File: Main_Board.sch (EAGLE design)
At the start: 189 parts, among them Q1 CSD17308Q3, Q2 CSD17308Q3, Q3 CSD17308Q3, Q4 CSD17308Q3, Q5 CSD17308Q3, Q6 CSD17308Q3, Q7 CSD17308Q3, U1 RN4020RN4020, U2 LMS8117, U3 5V_BUCK_REG, U4 IMU, U5 STM32F405RGT6, U6 TPA2005D1DGN, U7 BQ40Z60, U8 BQ2947, Y1 MC-30632.768K-E3, Y2 MA-5066-25.0000M-C0

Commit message: Finalized parts
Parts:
- added C14, C21: 4.7uF, SparkFun-Capacitors:CAP0805
- added C22: 150pF, SparkFun-Capacitors:CAP0805
- added C23: 10pF, SparkFun-Capacitors:CAP0805
- added C24: 47uF, BB8:CAP-1206
- added C25: 22uF, SparkFun-Capacitors:CAP0805
- added C53: 100nF, SparkFun-Capacitors:CAP0805
- added C55: 470nF, SparkFun-Capacitors:CAP0805
- added C58, C59: 0.1uF, SparkFun-Capacitors:CAP0805
- added J4: SPEAKER, BB8:2-PIN-JUMPER
- added J5: 5.5x2.1mm Barrel, SparkFun-Connectors:POWER_JACKSMD
- added J6: 9.7uH, BB8:2-PIN-JUMPER
- added L2: 3.3uH, BB8:INDUCTOR-SPM6530
- added Q8: SI9933CDY-PFET, BB8:SI9933CDY-PFET
- added R29: 57.6k, SparkFun-Passives:RESISTOR0805-RES
- added R30: 365k, SparkFun-Passives:RESISTOR0805-RES
- added R31: 113k, SparkFun-Passives:RESISTOR0805-RES
- added R61: 1.3M, SparkFun-Passives:RESISTOR0805-RES
- added R68: 1500, SparkFun-Passives:RESISTOR0805-RES
- added R70: 100k, SparkFun-Passives:RESISTOR0805-RES
- added RFOD: 196, SparkFun-Passives:RESISTOR0805-RES
- added ROS: 20k, SparkFun-Passives:RESISTOR0805-RES
- added U11: CBAT54S-SOT23-3, BB8:CBAT54S-SOT23-3
- added Z5: DDZ16ASF-7, BB8:DDZ16ASF-7
- C101: value (none) -> 270nF
- C102: value (none) -> 2.7nF
- C26, C27: value (none) -> 0.1uF
- CBOOT1, CBOOT2: value (none) -> 10nF
- CCLAMP1, CCLAMP2: value (none) -> 0.47uF
- CCOMM1, CCOMM2: value (none) -> 22nF
- D4: value BLUE -> GREEN
- D7: value 1N4148-0805 -> DIODE-1206; device BB8:1N4148-0805 -> BB8:DIODE-1206
- F1, F2: value F2875CT-ND -> (none)
- J2: value (none) -> SD_WP
- J3: value (none) -> BATTERY
- L3: device SparkFun-Passives:INDUCTOR0805 -> BB8:INDUCTOR-SPM6530
- R32: value (none) -> 66
- R33: value (none) -> 100k
- R34: value (none) -> 4.7k
- Y1: value MC-30632.768K-E3 -> (none)
- Y2: value MA-5066-25.0000M-C0 -> (none)
- renumbered U$10 to U10, U$12 to U12, U$9 to U9
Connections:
- removed net AUDIO_OUT+: U6.OUT+
- removed net AUDIO_OUT-: U6.OUT-
- removed net OUT: C26.1, D4.A, WPC-RX1.OUT
- removed net TRI-STATE: THM2.1, WPC-RX1.TS/CTRL
- removed net VDD_5V: C28.1, U6.VDD
- new net AUDIO+: J4.2, U6.OUT+
- new net AUDIO-: J4.1, U6.OUT-
- new net N$109: C53.2, U$5.CAP
- new net N$115: D4.C, R68.1
- new net N$117: R31.2, R61.1, U$5.FB
- new net N$119: C23.1, R30.2, U$5.VC
- new net N$120: C55.2, U11.P$3
- new net N$123: C24.2, U11.P$1, Z5.A
- new net N$124: C58.1, R33.1, R34.1, R70.1, WPC-RX1.TS/CTRL
- new net N$125: Q8G$1.G, Q8G$2.G, WPC-RX1.!AD-EN
- new net N$126: R34.2, THM2.1
- new net N$127: Q8G$1.S, Q8G$2.S
- new net N$128: C59.1, J5.PWR, Q8G$1.D, WPC-RX1.AD
- new net N$50: C22.1, R30.1
- new net N$51: C21.1, U$5.PWM/SYNC, U$5.VCC
- new net N$52: R29.2, U$5.RT
- new net N$53: C55.1, L2.2, U$5.SW
- new net WIRELESS_OUT_5V: C14.1, C26.1, D4.A, L2.1, Q8G$2.D, U$5.!SD, U$5.V_IN, WPC-RX1.OUT
- net 5V: now also C28.1, U6.VDD
- net AC2: now also J6.1
- net GND: now also C14.2, C21.2, C22.2, C23.2, C24.1, C25.2, C58.2, C59.2, J5.GND, J5.GNDBREAK, R29.1, R31.1, R70.2, RFOD.2, U$5.PGND, U$5.SGND, U11.P$2, Z5.C; no longer WPC-RX1.AD
- net N$59: now also J6.2
- net N$61: now also RFOD.1, ROS.1; no longer R33.1, R34.1
- net N$62: now also ROS.2; no longer R34.2
- net N$63: now also R68.2; no longer D4.C
- net PACK+: now also C25.1, C53.1, R61.2, U$5.V_OUT
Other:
- note added: "+15V Out, goes to Pack+"
- note added: "Is this okay kyle?"
- note added: "Wireless Charging Receiver and 5 to 15V Converter"
- note removed: "Coil goes here"
- note removed: "Wireless Charging Receiver"
- moved on the sheet: C28, D4, R33, R34, THM2, U$5

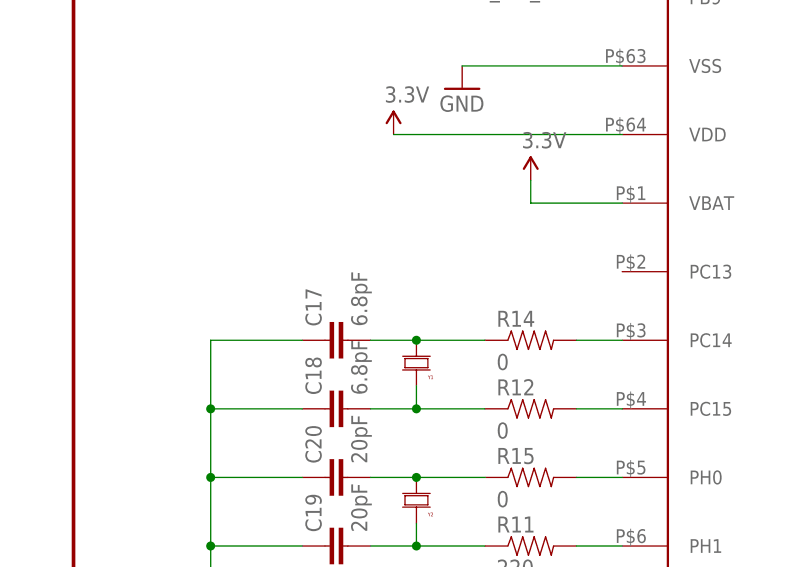
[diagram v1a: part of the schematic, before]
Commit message: added heartbeat LED to PC13
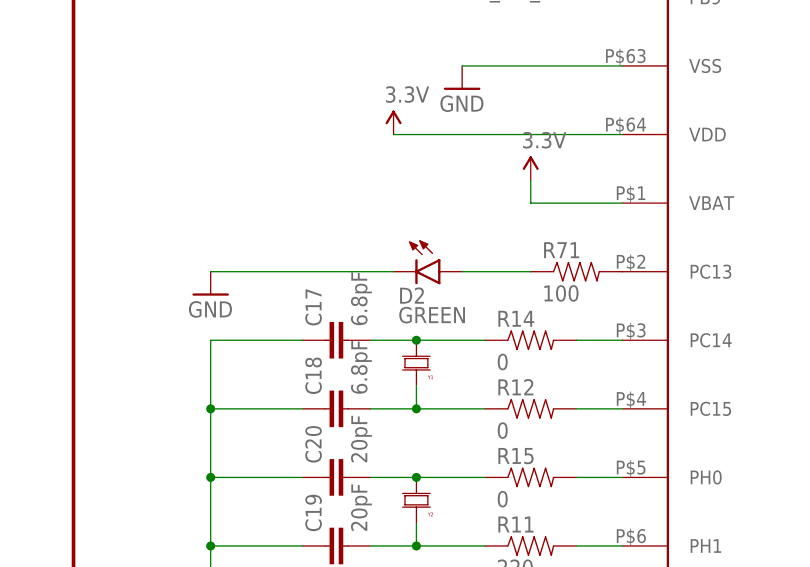
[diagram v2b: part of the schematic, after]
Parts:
- added D2: GREEN, SparkFun-LED:LED-BLUE0603
- added R71: 100, SparkFun-Resistors:RESISTOR0805-RES
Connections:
- new net N$129: R71.2, U5.PC13
- new net N$130: D2.A, R71.1
- net GND: now also D2.C
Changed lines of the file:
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@@
 <part name="J6" library="BB8" deviceset="2-PIN-JUMPER" device="" value="9.7uH"/>
 <part name="C24" library="BB8" deviceset="CAP-1206" device="" value="47uF"/>
+<part name="R71" library="SparkFun-Resistors" deviceset="RESISTOR" device="0805-RES" value="100"/>
+<part name="D2" library="SparkFun-LED" deviceset="LED-BLUE" device="0603" value="GREEN"/>
+<part name="GND48" library="SparkFun-Aesthetics" deviceset="GND" device=""/>
 </parts>
 <sheets>
@@
 <instance part="J6" gate="G$1" x="828.04" y="88.9"/>
 <instance part="C24" gate="G$1" x="1158.24" y="60.96" rot="R180"/>
+<instance part="R71" gate="G$1" x="330.2" y="134.62"/>
+<instance part="D2" gate="G$1" x="314.96" y="134.62" rot="R270"/>
+<instance part="GND48" gate="1" x="289.56" y="132.08"/>
 </instances>
 <busses>
@@
 <junction x="817.88" y="147.32"/>
 </segment>
+<segment>
+<pinref part="D2" gate="G$1" pin="C"/>
+<pinref part="GND48" gate="1" pin="GND"/>
+<wire x1="309.88" y1="134.62" x2="289.56" y2="134.62" width="0.1524" layer="91"/>
+</segment>
 </net>
 <net name="N$1" class="0">
@@
 </segment>
 </net>
+<net name="N$129" class="0">
+<segment>
+<pinref part="U5" gate="G$1" pin="PC13"/>
+<pinref part="R71" gate="G$1" pin="2"/>
+</segment>
+</net>
+<net name="N$130" class="0">
+<segment>
+<pinref part="R71" gate="G$1" pin="1"/>
+<pinref part="D2" gate="G$1" pin="A"/>
+<wire x1="325.12" y1="134.62" x2="317.5" y2="134.62" width="0.1524" layer="91"/>
+</segment>
+</net>

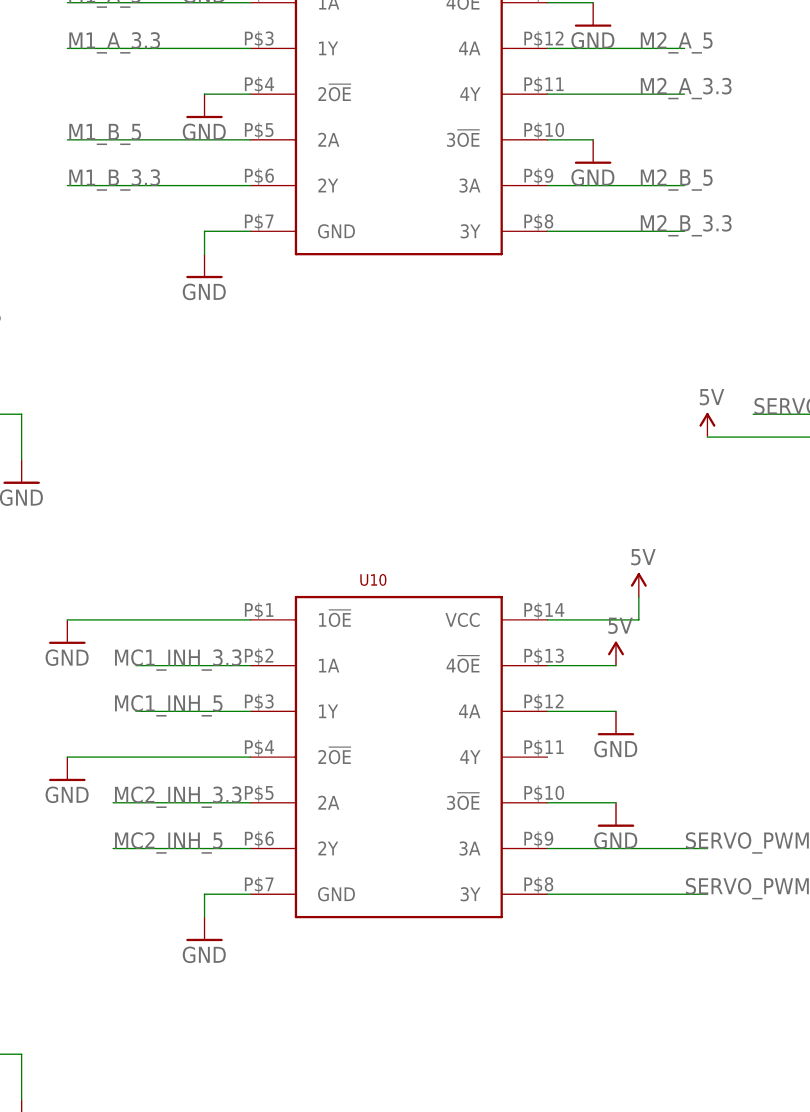
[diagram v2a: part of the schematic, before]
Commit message: Replaced inductor in buck regulator
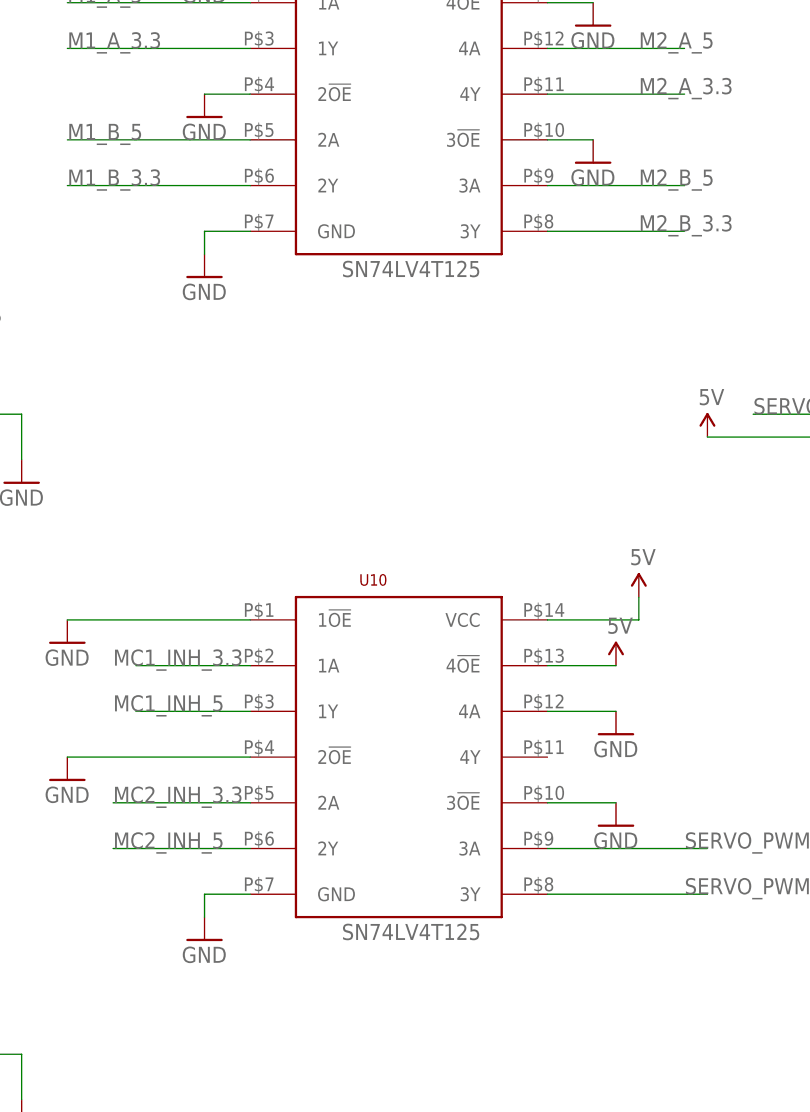
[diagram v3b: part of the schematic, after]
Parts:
- L1: device SparkFun-Passives:INDUCTOR0805 -> BB8:SRN840-101M
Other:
- note removed: "Change to Digikey Part#: SRN8040-101MCT-ND"
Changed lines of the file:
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@@
 <part name="U$8" library="BB8" deviceset="CAP_POL_PAN" device="" value="100uF"/>
 <part name="Z1" library="BB8" deviceset="SCHOTTKY_DIODE" device=""/>
-<part name="L1" library="SparkFun-Passives" deviceset="INDUCTOR" device="0805" value="100uH"/>
+<part name="L1" library="BB8" deviceset="SRN840-101M" device="" value="100uH"/>
 <part name="U$11" library="BB8" deviceset="CAP_POL_PAN" device="" value="470uF"/>
 <part name="GND34" library="SparkFun-Aesthetics" deviceset="GND" device=""/>
@@
 <text x="1663.7" y="-271.78" size="1.778" layer="97">also known as ground</text>
 <text x="1671.32" y="-248.92" size="1.778" layer="97">charging +</text>
-<text x="-5.08" y="-172.72" size="1.778" layer="98">Change to Digikey Part#:
-SRN8040-101MCT-ND</text>
 <text x="462.28" y="-220.98" size="1.778" layer="98">Should possibly be .065K</text>
 <text x="1056.64" y="101.6" size="1.778" layer="97">Is this okay kyle?</text>
@@
 <instance part="SUPPLY13" gate="G$1" x="-71.12" y="-91.44"/>
 <instance part="GND18" gate="1" x="-71.12" y="-106.68"/>
-<instance part="U9" gate="G$1" x="157.48" y="129.54"/>
+<instance part="U9" gate="G$1" x="167.64" y="114.3"/>
 <instance part="GND19" gate="1" x="147.32" y="93.98"/>
 <instance part="GND20" gate="1" x="147.32" y="111.76"/>
@@
 <instance part="GND23" gate="1" x="190.5" y="106.68"/>
 <instance part="SUPPLY14" gate="G$1" x="193.04" y="132.08"/>
-<instance part="U10" gate="G$1" x="157.48" y="55.88"/>
+<instance part="U10" gate="G$1" x="167.64" y="40.64"/>
 <instance part="SUPPLY15" gate="G$1" x="195.58" y="58.42"/>
 <instance part="GND24" gate="1" x="147.32" y="20.32"/>
@@
 </schematic>
 </drawing>
-<compatibility>
-<note version="6.3" minversion="6.2.2" severity="warning">
-Since Version 6.2.2 text objects can contain more than one line,
-which will not be processed correctly with this version.
-</note>
-</compatibility>
 </eagle>

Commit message: Renumbered ALL elements
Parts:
- removed C101: 270nF, SparkFun-Capacitors:CAP0805
- removed C102: 2.7nF, SparkFun-Capacitors:CAP0805
- removed CBOOT1, CBOOT2: 10nF, SparkFun-Capacitors:CAP0805
- removed CCLAMP1, CCLAMP2: 0.47uF, SparkFun-Capacitors:CAP0805
- removed CCOMM1, CCOMM2: 22nF, SparkFun-Capacitors:CAP0805
- removed D7: DIODE-1206, BB8:DIODE-1206
- removed RFOD: 196, SparkFun-Passives:RESISTOR0805-RES
- removed ROS: 20k, SparkFun-Passives:RESISTOR0805-RES
- removed THM2: 10K-NTC, BB8:THM
- removed U$1, U$2: BTM7752G, BB8:BTM7752G
- removed U$11, U$15: 470uF, BB8:CAP_POL_PAN
- removed U$13, U$14: 10uF, BB8:CAP_POL_PAN
- removed U$5: LTC3122-MSOP, BB8:LTC3122-MSOP
- removed U$6, U$7, U$8: 100uF, BB8:CAP_POL_PAN
- removed WPC-RX1: BQ51013B-20VQFN, BB8:BQ51013B-20VQFN
- added C60, C62, C64, C66, C67, C69, C73, C74: 0.1uF, SparkFun-Capacitors:CAP0805
- added C61, C68: 1uF, SparkFun-Capacitors:CAP0805
- added C63: 10uF, SparkFun-Capacitors:CAP0805
- added C65: 1.5uF, SparkFun-Capacitors:CAP0805
- added C70: 2.2uF, SparkFun-Capacitors:CAP0805
- added C71: 22pF, SparkFun-Capacitors:CAP0805
- added C72: 22uF, SparkFun-Capacitors:CAP0805
- added D3: BAS16-SOT3, BB8:BAS16-SOT3
- added P3: JTAG, BB8:JTAG
- added R72: 332k, SparkFun-Resistors:RESISTOR0805-RES
- added R73: 35.63k, SparkFun-Resistors:RESISTOR0805-RES
- added RT5: 10k, BB8:THM
- added U13: BQ2947, BB8:BQ2947
- added U14: TPA2005D1DGN, SparkFun-AnalogIC:TPA2005D1DGN
- added U15: BQ40Z60, BB8:BQ40Z60
- C1, C3: value 470nF -> 10uF; device SparkFun-Capacitors:CAP0805 -> BB8:CAP_POL_PAN
- C11: value 2.2uF -> .1uF; device SparkFun-Capacitors:CAP0805 -> SparkFun-Passives:CAP0805
- C12: value 2.2uF -> 6.8pF; device SparkFun-Capacitors:CAP0805 -> SparkFun-Passives:CAP0805
- C13: value 1uF -> 6.8pF; device SparkFun-Capacitors:CAP0805 -> SparkFun-Passives:CAP0805
- C14, C15: value 4.7uF -> 20pF; device SparkFun-Capacitors:CAP0805 -> SparkFun-Passives:CAP0805
- C16: value .1uF -> 100nF; device SparkFun-Passives:CAP0805 -> SparkFun-Capacitors:CAP0805
- C17, C18: value 6.8pF -> 2.2uF; device SparkFun-Passives:CAP0805 -> SparkFun-Capacitors:CAP0805
- C19: value 20pF -> 10uF; device SparkFun-Passives:CAP0805 -> SparkFun-Capacitors:CAP0805
- C2: value 10uF -> 100uF; device SparkFun-Capacitors:CAP0805 -> BB8:CAP_POL_PAN
- C20: value 20pF -> 100nF; device SparkFun-Passives:CAP0805 -> SparkFun-Capacitors:CAP0805
- C21: value 4.7uF -> 100nF
- C22: value 150pF -> 100nF
- C23: value 10pF -> 100nF
- C24: value 47uF -> 100nF; device BB8:CAP-1206 -> SparkFun-Capacitors:CAP0805
- C25: value 22uF -> 4.7uF
- C27: value 0.1uF -> 270nF
- C28: value 1uF -> 2.7nF
- C29, C32: value 0.1uF -> 22nF
- C30: value 0.1uF -> 10nF
- C31: value 22pF -> 10nF
- C33, C34: value 0.1uF -> 0.47uF
- C35: value 22uF -> 0.1uF
- C38: value 0.1uF -> 4.7uF
- C39: value 1.5uF -> 4.7uF
- C4, C5: value 100nF -> 100uF; device SparkFun-Capacitors:CAP0805 -> BB8:CAP_POL_PAN
- C40: value 2.2uF -> 150pF
- C41: value 10uF -> 100nF
- C42: value 0.1uF -> 470nF
- C43: value 0.1uF -> 10pF
- C44: value 0.1uF -> 47uF; device SparkFun-Capacitors:CAP0805 -> BB8:CAP-1206
- C45: value 2.2uF -> 22uF
- C53: value 100nF -> 0.1uF
- C55: value 470nF -> 0.1uF
- C56: value 0.1uF -> 2.2uF
- C6, C7: value 100nF -> 470nF
- C8, C9: value 100nF -> 470uF; device SparkFun-Capacitors:CAP0805 -> BB8:CAP_POL_PAN
- D1: value BAS16-SOT3 -> GREEN; device BB8:BAS16-SOT3 -> SparkFun-LED:LED-BLUE0603
- D4: value GREEN -> MBRA140; device SparkFun-LED:LED-BLUE0603 -> SparkFun-DiscreteSemi:MBRA140
- D5: value MBRA140 -> DIODE-1206; device SparkFun-DiscreteSemi:MBRA140 -> BB8:DIODE-1206
- J2: value SD_WP -> 5.5x2.1mm Barrel; device SparkFun-Connectors:M03PTH -> SparkFun-Connectors:POWER_JACKSMD
- J3: value BATTERY -> 9.7uH; device SparkFun-Connectors:M04JST -> BB8:2-PIN-JUMPER
- J4: value SPEAKER -> BATTERY; device BB8:2-PIN-JUMPER -> SparkFun-Connectors:M04JST
- J5: value 5.5x2.1mm Barrel -> SPEAKER; device SparkFun-Connectors:POWER_JACKSMD -> BB8:2-PIN-JUMPER
- J6: value 9.7uH -> SD_WP; device BB8:2-PIN-JUMPER -> SparkFun-Connectors:M03PTH
- Q1: value CSD17308Q3 -> SI9933CDY-PFET; device BB8:CSD17308Q3 -> BB8:SI9933CDY-PFET
- Q8: value SI9933CDY-PFET -> CSD17308Q3; device BB8:SI9933CDY-PFET -> BB8:CSD17308Q3
- R11: value 220 -> 10K
- R13: value 10K -> 0
- R15: value 0 -> 220
- R16: value 10K -> 100; device SparkFun-Passives:RESISTOR0805-RES -> SparkFun-Resistors:RESISTOR0805-RES
- R25: value 1k -> 10K; device SparkFun-Resistors:RESISTOR0805-RES -> SparkFun-Passives:RESISTOR0805-RES
- R26: value 100 -> 66; device SparkFun-Resistors:RESISTOR0805-RES -> SparkFun-Passives:RESISTOR0805-RES
- R27: value 1k -> 196; device SparkFun-Resistors:RESISTOR0805-RES -> SparkFun-Passives:RESISTOR0805-RES
- R28: value 1k -> 20k; device SparkFun-Resistors:RESISTOR0805-RES -> SparkFun-Passives:RESISTOR0805-RES
- R29: value 57.6k -> 4.7k
- R30: value 365k -> 100k
- R31: value 113k -> 100k
- R32: value 66 -> 1500
- R33: value 100k -> 57.6k
- R34: value 4.7k -> 365k
- R35: value 150k -> 1.3M
- R36: value 150k -> 113k
- R37, R41, R65: value 100 -> 1k
- R4: value .756K -> 4.7K
- R40, R62: value 100 -> 5.1k
- R42: value 100 -> 5m
- R43: value 100 -> 10
- R44: value 35.63k -> 150k; device SparkFun-Resistors:RESISTOR0805-RES -> SparkFun-Passives:RESISTOR0805-RES
- R45: value 332k -> 100
- R46: value 10m -> 100
- R47: value 10k -> 100
- R48, R49, R57: value 5.1k -> 100
- R5: value .244K -> 4.7K
- R50: value 1 -> 150k; device SparkFun-Resistors:RESISTOR0805-RES -> SparkFun-Passives:RESISTOR0805-RES
- R51: value 100k -> 5.1k
- R52: value 2 -> 10M
- R53: value 10M -> 5.1k
- R56: value 10k -> 5.1k
- R58: value 10M -> 100
- R59: value 5.1k -> 10M
- R60: value 10 -> 100
- R61: value 1.3M -> 10k; device SparkFun-Passives:RESISTOR0805-RES -> SparkFun-Resistors:RESISTOR0805-RES
- R66: value 5m -> 100
- R67: value 5.1k -> 1
- R68: value 1500 -> 100k; device SparkFun-Passives:RESISTOR0805-RES -> SparkFun-Resistors:RESISTOR0805-RES
- R69: value 100 -> 2
- R7: value 4.7K -> .756K
- R70: value 100k -> 10m; device SparkFun-Passives:RESISTOR0805-RES -> SparkFun-Resistors:RESISTOR0805-RES
- R71: value 100 -> 10k
- R8: value 4.7K -> .768K
- R9: value .768K -> .244K
- RT1: value 10k-NTC -> 10K-NTC
- RT2: value 10k -> 10k-NTC
- U1: value RN4020RN4020 -> LMS8117; device BB8:RN4020RN4020 -> BB8:LMS8117
- U10: value SN74LV4T125 -> IMU; device BB8:SN74LV4T125 -> BB8:IMU
- U11: value CBAT54S-SOT23-3 -> LTC3122-MSOP; device BB8:CBAT54S-SOT23-3 -> BB8:LTC3122-MSOP
- U12: value JTAG -> CBAT54S-SOT23-3; device BB8:JTAG -> BB8:CBAT54S-SOT23-3
- U2: value LMS8117 -> 5V_BUCK_REG; device BB8:LMS8117 -> BB8:5V_BUCK_REG
- U3: value 5V_BUCK_REG -> BTM7752G; device BB8:5V_BUCK_REG -> BB8:BTM7752G
- U4: value IMU -> BTM7752G; device BB8:IMU -> BB8:BTM7752G
- U5: value STM32F405RGT6 -> SN74LV4T125; device BB8:STM32F405RGT6 -> BB8:SN74LV4T125
- U6: value TPA2005D1DGN -> SN74LV4T125; device SparkFun-AnalogIC:TPA2005D1DGN -> BB8:SN74LV4T125
- U7: value BQ40Z60 -> STM32F405RGT6; device BB8:BQ40Z60 -> BB8:STM32F405RGT6
- U8: value BQ2947 -> RN4020RN4020; device BB8:BQ2947 -> BB8:RN4020RN4020
- U9: value SN74LV4T125 -> BQ51013B-20VQFN; device BB8:SN74LV4T125 -> BB8:BQ51013B-20VQFN
- Z2: value MM3Z75VC -> DDZ16ASF-7; device BB8:MM3Z75VC -> BB8:DDZ16ASF-7
- Z5: value DDZ16ASF-7 -> MM3Z75VC; device BB8:DDZ16ASF-7 -> BB8:MM3Z75VC
- renumbered S2 to S1, SD1 to P4, U$3 to P1, U$4 to P2
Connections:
- net !NRST: now also P3.NRST, U7.!RST; no longer U12.NRST, U5.!RST
- net 3.3V: now also C16.2, C19.1, C20.1, C21.1, C22.1, C23.1, C24.1, C25.2, C3.+, P3.VDD, P3.VDD@2, U1.VOUT, U10.CS_AG, U10.CS_M, U10.VCC, U5.VCC, U7.VBAT, U7.VDD, U7.VDD@32, U7.VDD@48, U7.VDD@64, U7.VDDA, U8.VDD; no longer C15.2, C2.1, C4.1, C5.1, C6.1, C7.1, C8.1, C9.2, U$14.+, U1.VDD, U12.VDD, U12.VDD@2, U2.VOUT, U4.CS_AG, U4.CS_M, U4.VCC, U5.VBAT, U5.VDD, U5.VDD@32, U5.VDD@48, U5.VDD@64, U5.VDDA, U9.VCC
- net 5V: now also C1.+, C61.1, U1.VIN, U14.VDD, U6.4!OE, U6.VCC; no longer C28.1, U$13.+, U10.4!OE, U10.VCC, U2.VIN, U6.VDD
- net AC1: now also C27.2, C28.1, C29.1, C30.1, C34.1, U9.AC1; no longer C101.2, C102.1, CBOOT1.1, CCLAMP1.1, CCOMM1.1, WPC-RX1.AC1
- net AC2: now also C28.2, C31.1, C32.1, C33.1, J3.1, U9.AC2; no longer C102.2, CBOOT2.1, CCLAMP2.1, CCOMM2.1, J6.1, WPC-RX1.AC2
- net AUDIO+: now also J5.2, U14.OUT+; no longer J4.2, U6.OUT+
- net AUDIO-: now also J5.1, U14.OUT-; no longer J4.1, U6.OUT-
- net AUDIO_PWM: now also C50.1, U7.PA5; no longer C29.1, U5.PA5
- net BLUE_WAKE_SW: now also U7.PA4, U8.WAKE_SW; no longer U1.WAKE_SW, U5.PA4
- net BLU_CMD: now also U7.PB1, U8.CMD/MLDP; no longer U1.CMD/MLDP, U5.PB1
- net BLU_CTS: now also U7.PA1, U8.PIO5; no longer U1.PIO5, U5.PA1
- net BLU_RTS: now also U7.PA0_WKUP, U8.RTS/PIO6; no longer U1.RTS/PIO6, U5.PA0_WKUP
- net BLU_RX: now also U7.PA2, U8.UART_RX; no longer U1.UART_RX, U5.PA2
- net BLU_TX: now also U7.PA3, U8.UART_TX; no longer U1.UART_TX, U5.PA3
- net BLU_WAKE_HW: now also U7.PA6, U8.WAKE_HW; no longer U1.WAKE_HW, U5.PA6
- net BOOT2: now also C31.2, U9.BOOT2; no longer CBOOT2.2, WPC-RX1.BOOT2
- net CHRG_GPIO_SYSPRES: now also R65.2, U7.PA9; no longer R38.2, U5.PA9
- net CHRG_I2C_SCL: now also R63.2, U7.PB10; no longer R43.2, U5.PB10
- net CHRG_I2C_SDA: now also R64.2, U7.PB11; no longer R41.2, U5.PB11
- net CHRG_I2C_SMBA: now also R66.2, U7.PB12; no longer R37.2, U5.PB12
- net GND: now also C1.-, C11.1, C12.1, C14.1, C17.2, C18.2, C19.2, C2.-, C20.2, C24.2, C25.1, C3.-, C35.2, C36.2, C37.2, C38.2, C4.-, C40.2, C43.2, C44.1, C46.2, C49.1, C5.-, C55.2, C56.2, C61.2, C63.1, C65.2, C66.2, C67.2, C68.1, C74.1, C8.-, C9.-, D1.C, J2.GND, J2.GNDBREAK, J4.4, P3.GND, P3.GND@10, P3.GND@12, P3.GND@14, P3.GND@16, P3.GND@18, P3.GND@20, P3.GND@6, P3.GND@8, Q2.S1, R24.1, R27.2, R30.2, R31.2, R33.1, R36.1, R42.1, R49.1, R51.2, R71.2, R73.1, R9.2, RT5.2, U1.ADJ/GND, U11.PGND, U11.SGND, U12.P$2, U13.GNDPAD, U13.VSS, U14.GND@1, U14.GND@2, U15.PGND, U15.VSS, U2.!ON/OFF, U2.GND, U3.GND@23, U3.GND@24, U3.GND@25, U3.GND@26, U3.GND@6, U3.GND@7, U3.GND@8, U4.GND@23, U4.GND@24, U4.GND@25, U4.GND@26, U4.GND@6, U4.GND@7, U4.GND@8, U5.1!OE, U5.2!OE, U5.3!OE, U5.4!OE, U5.GND, U6.1!OE, U6.2!OE, U6.3!OE, U6.4A, U6.GND, U7.VSS@63, U7.VSSA, U8.GND@1, U8.GND@24, U9.PGND, Z2.C, Z5.A; no longer C1.2, C12.2, C14.2, C16.2, C17.1, C18.1, C19.1, C2.2, C20.1, C24.1, C25.2, C27.2, C28.2, C3.2, C30.2, C32.2, C33.2, C37.1, C4.2, C41.1, C44.2, C49.2, C5.2, C52.2, C56.1, C8.2, C9.1, D2.C, J3.4, J5.GND, J5.GNDBREAK, Q7.S1, R16.1, R29.1, R31.1, R33.2, R44.1, R47.2, R5.2, R59.2, R65.1, R66.1, R70.2, RFOD.2, THM2.2, U$1.GND, U$1.GND@23, U$1.GND@24, U$1.GND@25, U$1.GND@26, U$1.GND@6, U$1.GND@7, U$1.GND@8, U$11.-, U$13.-, U$14.-, U$15.-, U$2.GND, U$2.GND@23, U$2.GND@24, U$2.GND@25, U$2.GND@26, U$2.GND@6, U$2.GND@7, U$2.GND@8, U$5.PGND, U$5.SGND, U$6.-, U$7.-, U$8.-, U1.GND@1, U1.GND@24, U10.1!OE, U10.2!OE, U10.3!OE, U10.4A, U11.P$2, U12.GND, U12.GND@10, U12.GND@12, U12.GND@14, U12.GND@16, U12.GND@18, U12.GND@20, U12.GND@6, U12.GND@8, U2.ADJ/GND, U3.!ON/OFF, U5.VSS, U5.VSS@63, U5.VSSA, U6.GND@1, U6.GND@2, U7.PGND, U8.GNDPAD, U8.VSS, U9.1!OE, U9.2!OE, U9.3!OE, U9.4!OE, U9.GND, WPC-RX1.PGND, Z2.A, Z5.C
- net IMU_I2C_SCL: now also U10.SCL, U7.PB6; no longer U4.SCL, U5.PB6
- net IMU_I2C_SDA: now also U10.SDA, U7.PB7; no longer U4.SDA, U5.PB7
- net JNTRST: now also P3.JNTRST, U7.PB4; no longer U12.JNTRST, U5.PB4
- net JTCK: now also P3.JTCK, U7.PA14; no longer U12.JTCK, U5.PA14
- net JTDI: now also P3.JTDI, U7.PA15; no longer U12.JTDI, U5.PA15
- net JTDO: now also P3.JTDO, U7.PB3; no longer U12.JTDO, U5.PB3
- net JTMS: now also P3.JTMS, U7.PA13; no longer U12.JTMS, U5.PA13
- net M1_A_3.3: now also U5.1Y, U7.PA7; no longer U5.PA7, U9.1Y
- net M1_A_5: now also U5.1A; no longer U9.1A
- net M1_B_3.3: now also U5.2Y, U7.PC4; no longer U5.PC4, U9.2Y
- net M1_B_5: now also U5.2A; no longer U9.2A
- net M2_A_3.3: now also U5.4Y, U7.PC5; no longer U5.PC5, U9.4Y
- net M2_A_5: now also U5.4A; no longer U9.4A
- net M2_B_3.3: now also U5.3Y, U7.PB0; no longer U5.PB0, U9.3Y
- net M2_B_5: now also U5.3A; no longer U9.3A
- net MC1_IN1: now also U7.PC7; no longer U5.PC7
- net MC1_IN2: now also R3.1, U7.PC6; no longer R2.1, U5.PC6
- net MC1_INH_3.3: now also U6.1A, U7.PC9; no longer U10.1A, U5.PC9
- net MC1_INH_5: now also R5.2, U6.1Y; no longer R3.2, U10.1Y
- net MC1_IS: now also R7.2, R9.1, U7.PC0; no longer R4.2, R5.1, U5.PC0
- net MC2_IN1: now also R2.1, U7.PB15; no longer R6.1, U5.PB15
- net MC2_IN2: now also R4.1, U7.PB14; no longer R7.1, U5.PB14
- net MC2_INH_3.3: now also U6.2A, U7.PC8; no longer U10.2A, U5.PC8
- net MC2_INH_5: now also R6.2, U6.2Y; no longer R8.2, U10.2Y
- net MC2_IS: now also R8.2, U7.PC1; no longer R9.2, U5.PC1
- net N$1: now also U3.OUT1, U3.OUT1@2, U3.OUT1@3, U3.OUT1@33, U3.OUT1@34, U3.OUT1@35, U3.OUT1@36, U3.OUT1@4; no longer U$1.OUT1, U$1.OUT1@2, U$1.OUT1@3, U$1.OUT1@33, U$1.OUT1@34, U$1.OUT1@35, U$1.OUT1@36, U$1.OUT1@4
- net N$10: now also R2.2, U4.IN1; no longer R6.2, U$2.IN1
- net N$100: now also C60.2, C62.1; no longer C42.2, C43.1
- net N$101: now also C60.1, Q3.S1, R52.1; no longer C42.1, Q5.S1, R58.1
- net N$102: now also Q3.G1, R52.2, R53.1; no longer Q5.G1, R57.1, R58.2
- net N$103: now also R53.2, U15.CHG; no longer R57.2, U7.CHG
- net N$104: now also J4.1, R37.1, R39.2, R43.1, R45.1; no longer J3.1, R25.1, R60.1, R62.1, R69.2
- net N$105: now also D3.P$3, U15.BAT; no longer D1.P$3, U7.BAT
- net N$106: now also D3.P$1, R43.2; no longer D1.P$1, R60.2
- net N$107: now also C56.1, U15.PBI; no longer C45.1, U7.PBI
- net N$108: now also C54.1, R45.2, U15.VC3, U15.VC4; no longer C46.1, R62.2, U7.VC3, U7.VC4
- net N$109: now also C41.2, U11.CAP; no longer C53.2, U$5.CAP
- net N$11: now also R4.2, U4.IN2; no longer R7.2, U$2.IN2
- net N$110: now also C53.1, C54.2, R46.2, U15.VC2; no longer C46.2, C47.1, R63.2, U7.VC2
- net N$111: now also C53.2, C57.1, R47.2, U15.VC1; no longer C47.2, C48.1, R26.2, U7.VC1
- net N$112: now also C52.1, C58.1, R48.2, U15.SRN; no longer C49.1, C50.1, R64.2, U7.SRN
- net N$113: now also C52.2, C59.1, R49.2, U15.SRP; no longer C50.2, C51.1, R65.2, U7.SRP
- net N$114: now also R40.1, U13.OUT; no longer R67.1, U8.OUT
- net N$115: now also D2.C, R32.1; no longer D4.C, R68.1
- net N$116: now also J4.2, R38.1, R46.1; no longer J3.2, R28.1, R63.1
- net N$117: now also R35.1, R36.2, U11.FB; no longer R31.2, R61.1, U$5.FB
- net N$118: now also C46.1, R39.1, U13.VDD; no longer C52.1, R69.1, U8.VDD
- net N$119: now also C43.1, R34.2, U11.VC; no longer C23.1, R30.2, U$5.VC
- net N$12: now also C12.2, R12.1; no longer C17.2, R14.1
- net N$120: now also C42.2, U12.P$3; no longer C55.2, U11.P$3
- net N$121: now also C49.2, R41.1, U13.V1; no longer C56.2, R27.1, U8.V1
- net N$122: now also C48.1, U13.CD; no longer C57.1, U8.CD
- net N$123: now also C44.2, U12.P$1, Z2.A; no longer C24.2, U11.P$1, Z5.A
- net N$124: now also C37.1, R29.1, R30.1, R31.1, U9.TS/CTRL; no longer C58.1, R33.1, R34.1, R70.1, WPC-RX1.TS/CTRL
- net N$125: now also Q1G$1.G, Q1G$2.G, U9.!AD-EN; no longer Q8G$1.G, Q8G$2.G, WPC-RX1.!AD-EN
- net N$126: now also R29.2, RT1.1; no longer R34.2, THM2.1
- net N$127: now also Q1G$1.S, Q1G$2.S; no longer Q8G$1.S, Q8G$2.S
- net N$128: now also C26.1, J2.PWR, Q1G$1.D, U9.AD; no longer C59.1, J5.PWR, Q8G$1.D, WPC-RX1.AD
- net N$129: now also R16.2, U7.PC13; no longer R71.2, U5.PC13
- net N$13: now also R8.1, U4.IS; no longer R9.1, U$2.IS
- net N$130: now also D1.A, R16.1; no longer D2.A, R71.1
- net N$14: now also R6.1, U4.INH; no longer R8.1, U$2.INH
- net N$15: now also C17.1, U7.VCAP_2; no longer C12.1, U5.VCAP_2
- net N$16: now also C18.1, U7.VCAP_1; no longer C11.1, U5.VCAP_1
- net N$17: now also C15.2, R15.1; no longer C19.2, R11.1
- net N$18: now also C13.2, R13.1; no longer C18.2, R12.1
- net N$19: now also R15.2, U7.PH1; no longer R11.2, U5.PH1
- net N$2: now also U3.OUT2, U3.OUT2@16, U3.OUT2@17, U3.OUT2@18, U3.OUT2@19, U3.OUT2@20, U3.OUT2@21, U3.OUT2@22; no longer U$1.OUT2, U$1.OUT2@16, U$1.OUT2@17, U$1.OUT2@18, U$1.OUT2@19, U$1.OUT2@20, U$1.OUT2@21, U$1.OUT2@22
- net N$20: now also C14.2, R14.1; no longer C20.2, R15.1
- net N$21: now also R13.2, U7.PC15; no longer R12.2, U5.PC15
- net N$22: now also R11.2, U7.BOOT0; no longer R13.2, U5.BOOT0
- net N$23: now also R11.1; no longer R13.1
- net N$24: now also P3.P$11, R20.2; no longer R16.2, U12.P$11
- net N$25: now also P3.P$17, R21.2; no longer R17.2, U12.P$17
- net N$26: now also P3.P$19, R24.2; no longer R18.2, U12.P$19
- net N$28: now also R17.2, U8.AIO0; no longer R21.2, U1.AIO0
- net N$29: now also R12.2, U7.PC14; no longer R14.2, U5.PC14
- net N$3: now also U3.IN1; no longer U$1.IN1
- net N$30: now also R14.2, U7.PH0; no longer R15.2, U5.PH0
- net N$31: now also U2.OUTPUT; no longer U3.OUTPUT
- net N$32: now also C8.+, C9.+, U2.FEEDBACK; no longer U$11.+, U$15.+, U3.FEEDBACK
- net N$33: now also J4.3, R41.2, R47.1; no longer J3.3, R26.1, R27.2
- net N$34: now also U8.PIO1; no longer U1.PIO1
- net N$36: now also U8.PIO2; no longer U1.PIO2
- net N$37: now also R25.2, U8.PIO3; no longer R24.2, U1.PIO3
- net N$39: now also R25.1; no longer R24.1
- net N$4: now also R3.2, U3.IN2; no longer R2.2, U$1.IN2
- net N$40: now also C47.1, R37.2, U13.V3, U13.V4; no longer C54.1, R25.2, U8.V3, U8.V4
- net N$41: now also J6.1; no longer J2.1
- net N$42: now also J6.3; no longer J2.3
- net N$43: now also U10.DEN; no longer U4.DEN
- net N$44: now also U10.INT2; no longer U4.INT2
- net N$45: now also U10.INT1; no longer U4.INT1
- net N$46: now also C47.2, R38.2, U13.V2; no longer C54.2, R28.2, U8.V2
- net N$47: now also U10.SDO_AG, U10.SDO_M; no longer U4.SDO_AG, U4.SDO_M
- net N$48: now also R18.2, U8.AIO1; no longer R20.2, U1.AIO1
- net N$49: now also Q2.D1; no longer Q7.D1
- net N$5: now also R7.1, U3.IS; no longer R4.1, U$1.IS
- net N$50: now also C40.1, R34.1; no longer C22.1, R30.1
- net N$51: now also C39.1, U11.PWM/SYNC, U11.VCC; no longer C21.1, U$5.PWM/SYNC, U$5.VCC
- net N$52: now also R33.2, U11.RT; no longer R29.2, U$5.RT
- net N$53: now also C42.1, U11.SW; no longer C55.1, U$5.SW
- net N$54: now also C32.2, U9.COMM2; no longer CCOMM2.2, WPC-RX1.COMM2
- net N$55: now also C33.2, U9.CLAMP2; no longer CCLAMP2.2, WPC-RX1.CLAMP2
- net N$56: now also C34.2, U9.CLAMP1; no longer CCLAMP1.2, WPC-RX1.CLAMP1
- net N$57: now also C30.2, U9.BOOT1; no longer CBOOT1.2, WPC-RX1.BOOT1
- net N$58: now also C29.2, U9.COMM1; no longer CCOMM1.2, WPC-RX1.COMM1
- net N$59: now also C27.1, J3.2; no longer C101.1, J6.2
- net N$6: now also R5.1, U3.INH; no longer R3.1, U$1.INH
- net N$60: now also R26.1, U9.ILIM; no longer R32.1, WPC-RX1.ILIM
- net N$61: now also R26.2, R27.1, R28.1, U9.FOD; no longer R32.2, RFOD.1, ROS.1, WPC-RX1.FOD
- net N$62: now also C35.1, R28.2, U9.RECT; no longer C27.1, ROS.2, WPC-RX1.RECT
- net N$63: now also R32.2, U9.!CHG; no longer R68.2, WPC-RX1.!CHG
- net N$64: now also R50.2, U14.IN-; no longer R36.2, U6.IN-
- net N$65: now also C50.2, R44.1; no longer C29.2, R35.1
- net N$66: now also C51.1, R50.1; no longer C30.1, R36.1
- net N$67: now also R44.2, U14.IN+; no longer R35.2, U6.IN+
- net N$68: now also RT2.1, U15.TS1; no longer RT1.1, U7.TS1
- net N$69: now also RT3.1, U15.TS2; no longer RT2.1, U7.TS2
- net N$7: now also U8.AIO2; no longer U1.AIO2
- net N$70: now also RT4.1, U15.TS3; no longer RT3.1, U7.TS3
- net N$71: now also RT5.1, U15.TS4; no longer RT4.1, U7.TS4
- net N$72: now also R66.1, U15.ALERT/BTP; no longer R37.1, U7.ALERT/BTP
- net N$73: now also R57.1, U15.SYSPRES; no longer R39.1, U7.SYSPRES
- net N$74: now also R57.2, R65.1, Z3.C; no longer R38.1, R39.2, Z2.C
- net N$75: now also R58.1, U15.SMBD; no longer R40.1, U7.SMBD
- net N$76: now also R58.2, R64.1, Z4.C; no longer R40.2, R41.1, Z3.C
- net N$77: now also R60.1, U15.SMBC; no longer R42.1, U7.SMBC
- net N$78: now also R60.2, R63.1, Z5.C; no longer R42.2, R43.1, Z4.C
- net N$79: now also C71.1, R72.1, R73.2, U15.VFB; no longer C31.1, R44.2, R45.1, U7.VFB
- net N$8: now also U4.OUT1, U4.OUT1@2, U4.OUT1@3, U4.OUT1@33, U4.OUT1@34, U4.OUT1@35, U4.OUT1@36, U4.OUT1@4; no longer U$2.OUT1, U$2.OUT1@2, U$2.OUT1@3, U$2.OUT1@33, U$2.OUT1@34, U$2.OUT1@35, U$2.OUT1@36, U$2.OUT1@4
- net N$80: now also C66.1, C69.2, Q5.S1, R70.2, U15.HSRP; no longer C33.1, C34.2, Q6.S1, R46.2, U7.HSRP
- net N$81: now also Q8.G1, R71.1; no longer Q1.G1, R47.1
- net N$82: now also Q6.G1, Q8.D1, R56.1, R59.2; no longer Q1.D1, Q3.G1, R48.1, R53.2
- net N$83: now also R56.2, U15.ACFET; no longer R48.2, U7.ACFET
- net N$84: now also C73.1, C74.2; no longer C36.1, C37.2
- net N$85: now also C64.1, D4.C, U15.BTST; no longer C38.1, D5.C, U7.BTST
- net N$86: now also C65.1, D4.A, U15.REGN; no longer C39.1, D5.A, U7.REGN
- net N$87: now also C64.2, Q7.D1, U15.PH; no longer C38.2, Q2.D1, U7.PH
- net N$88: now also C55.1, Q2.G1, R40.2, R51.1, R62.2; no longer C44.1, Q7.G1, R49.2, R59.1, R67.2
- net N$89: now also C68.2, R67.1, U15.VCC; no longer C13.2, R50.1, U7.VCC
- net N$9: now also U4.OUT2, U4.OUT2@16, U4.OUT2@17, U4.OUT2@18, U4.OUT2@19, U4.OUT2@20, U4.OUT2@21, U4.OUT2@22; no longer U$2.OUT2, U$2.OUT2@16, U$2.OUT2@17, U$2.OUT2@18, U$2.OUT2@19, U$2.OUT2@20, U$2.OUT2@21, U$2.OUT2@22
- net N$90: now also R62.1, U15.AFEFUSE; no longer R49.1, U7.AFEFUSE
- net N$91: now also D5.C; no longer D7.C
- net N$92: now also C70.2, R69.2; no longer C40.2, R52.2
- net N$93: now also Q7.G1, U15.LODRV; no longer Q2.G1, U7.LODRV
- net N$94: now also C63.2, Q5.D1, R67.2; no longer C41.2, Q3.D1, R50.2
- net N$95: now also Q5.G1, U15.HIDRV; no longer Q6.G1, U7.HIDRV
- net N$96: now also U15.DSG; no longer U7.DSG
- net N$98: now also R61.2, U15.ACP; no longer R56.2, U7.ACP
- net N$99: now also Q3.D1; no longer Q5.D1
- net PACK+: now also C41.1, C45.1, C73.2, D5.A, Q6.S1, Q8.S1, R35.2, R59.1, R61.1, R68.1, R69.1, U11.V_OUT; no longer C25.1, C36.2, C53.1, D7.A, Q1.S1, Q3.S1, R51.1, R52.1, R53.1, R56.1, R61.2, U$5.V_OUT
- net PACK-: now also R42.2, R48.1; no longer R64.1, R66.2
- net PGND: now also C70.1, C72.1, Q7.S1, R68.2; no longer C35.1, C40.1, Q2.S1, R51.2
- net SD_SPI_MISO: now also U7.PC2; no longer U5.PC2
- net SD_SPI_MOSI: now also U7.PC3; no longer U5.PC3
- net SD_SPI_NSS: now also U7.PB9; no longer U5.PB9
- net SD_SPI_SCK: now also U7.PB13; no longer U5.PB13
- net SERVO_PWM_3.3: now also U6.3A, U7.PA8; no longer U10.3A, U5.PA8
- net SERVO_PWM_5: now also U6.3Y; no longer U10.3Y
- net SPEAKER_SHUTDOWN: now also U14.SHUTDOWN, U7.PB2; no longer U5.PB2, U6.SHUTDOWN
- net SYSTEMLOAD: now also C62.2, C67.1, C69.1, C71.2, C72.2, R70.1, R72.2, U15.HSRN; no longer C31.2, C32.1, C34.1, C35.2, C43.2, R45.2, R46.1, U7.HSRN
- net VCC: now also C2.+, C4.+, C5.+, C6.1, C7.1, U2.VIN, U3.VS, U3.VS@12, U3.VS@13, U3.VS@14, U3.VS@29, U3.VS@30, U3.VS@31, U3.VS@32, U4.VS, U4.VS@12, U4.VS@13, U4.VS@14, U4.VS@29, U4.VS@30, U4.VS@31, U4.VS@32; no longer C1.1, C3.1, U$1.VS, U$1.VS@12, U$1.VS@13, U$1.VS@14, U$1.VS@29, U$1.VS@30, U$1.VS@31, U$1.VS@32, U$2.VS, U$2.VS@12, U$2.VS@13, U$2.VS@14, U$2.VS@29, U$2.VS@30, U$2.VS@31, U$2.VS@32, U$6.+, U$7.+, U$8.+, U3.VIN
- net WIRELESS_EN1: now also U7.PA10, U9.EN1; no longer U5.PA10, WPC-RX1.EN1
- net WIRELESS_EN2: now also U7.PA11, U9.EN2; no longer U5.PA11, WPC-RX1.EN2
- net WIRELESS_OUT_5V: now also C36.1, C38.1, D2.A, Q1G$2.D, U11.!SD, U11.V_IN, U9.OUT; no longer C14.1, C26.1, D4.A, Q8G$2.D, U$5.!SD, U$5.V_IN, WPC-RX1.OUT
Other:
- moved on the sheet: C11, C12, C13, C14, C15, C16, C17, C18, C19, C20, C21, C22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

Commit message: Minor moving around
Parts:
- F1, F2: value (none) -> 4A
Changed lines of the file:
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@@
 <part name="D3" library="BB8" deviceset="BAS16-SOT3" device=""/>
 <part name="U11" library="BB8" deviceset="LTC3122-MSOP" device=""/>
-<part name="F1" library="BB8" deviceset="F2875CT-ND" device=""/>
-<part name="F2" library="BB8" deviceset="F2875CT-ND" device=""/>
+<part name="F1" library="BB8" deviceset="F2875CT-ND" device="" value="4A"/>
+<part name="F2" library="BB8" deviceset="F2875CT-ND" device="" value="4A"/>
 <part name="L2" library="BB8" deviceset="INDUCTOR-SPM6530" device="" value="3.3uH"/>
 <part name="C38" library="SparkFun-Capacitors" deviceset="CAP" device="0805" value="4.7uF"/>

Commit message: Preliminary layout for wireless receiver done
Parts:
- D5: value DIODE-1206 -> D-1206; device BB8:DIODE-1206 -> BB8:D-1206
- J6: device SparkFun-Connectors:M03PTH -> SparkFun-Connectors:M02PTH
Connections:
- net N$42: now also J6.2; no longer J6.3
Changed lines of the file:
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@@
 <part name="R67" library="SparkFun-Resistors" deviceset="RESISTOR" device="0805-RES" value="1"/>
 <part name="D6" library="SparkFun-DiscreteSemi" deviceset="DIODE-SCHOTTKY" device="-MBRA140" value="MBRA140"/>
-<part name="D5" library="BB8" deviceset="DIODE-1206" device=""/>
+<part name="D5" library="BB8" deviceset="D-1206" device=""/>
 <part name="C70" library="SparkFun-Capacitors" deviceset="CAP" device="0805" value="2.2uF"/>
 <part name="R68" library="SparkFun-Resistors" deviceset="RESISTOR" device="0805-RES" value="100k"/>
@@
 <part name="R37" library="SparkFun-Resistors" deviceset="RESISTOR" device="0805-RES" value="1k"/>
 <part name="R47" library="SparkFun-Resistors" deviceset="RESISTOR" device="0805-RES" value="100"/>
-<part name="J6" library="SparkFun-Connectors" deviceset="M03" device="PTH" value="SD_WP"/>
 <part name="GND49" library="SparkFun-Aesthetics" deviceset="GND" device=""/>
 <part name="SUPPLY22" library="SparkFun-Aesthetics" deviceset="3.3V" device=""/>
@@
 <part name="D1" library="SparkFun-LED" deviceset="LED-BLUE" device="0603" value="GREEN"/>
 <part name="GND28" library="SparkFun-Aesthetics" deviceset="GND" device=""/>
+<part name="J6" library="SparkFun-Connectors" deviceset="M02" device="PTH" value="SD_WP"/>
 </parts>
 <sheets>
@@
 <instance part="R37" gate="G$1" x="1292.86" y="-160.02" rot="R270"/>
 <instance part="R47" gate="G$1" x="1422.4" y="-185.42"/>
-<instance part="J6" gate="J$1" x="1643.38" y="124.46" rot="R180"/>
 <instance part="GND49" gate="1" x="982.98" y="-149.86" rot="R180"/>
 <instance part="SUPPLY22" gate="G$1" x="975.36" y="-162.56"/>
@@
 <instance part="D1" gate="G$1" x="314.96" y="134.62" rot="R270"/>
 <instance part="GND28" gate="1" x="289.56" y="132.08"/>
+<instance part="J6" gate="G$1" x="1645.92" y="124.46" rot="R180"/>
 </instances>
 <busses>
@@
 <segment>
 <pinref part="P4" gate="G$1" pin="WP"/>
-<pinref part="J6" gate="J$1" pin="1"/>
-<wire x1="1620.52" y1="127" x2="1635.76" y2="127" width="0.1524" layer="91"/>
+<wire x1="1620.52" y1="127" x2="1638.3" y2="127" width="0.1524" layer="91"/>
+<pinref part="J6" gate="G$1" pin="1"/>
+<wire x1="1638.3" y1="127" x2="1638.3" y2="124.46" width="0.1524" layer="91"/>
 </segment>
 </net>
@@
 <segment>
 <pinref part="P4" gate="G$1" pin="COM"/>
-<pinref part="J6" gate="J$1" pin="3"/>
-<wire x1="1620.52" y1="121.92" x2="1635.76" y2="121.92" width="0.1524" layer="91"/>
+<wire x1="1620.52" y1="121.92" x2="1638.3" y2="121.92" width="0.1524" layer="91"/>
+<pinref part="J6" gate="G$1" pin="2"/>
 </segment>
 </net>

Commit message: More board movement, things are now more or less clustered now
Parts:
- J1: value (none) -> SERVO
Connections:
- removed net SYSTEMLOAD: C62.2, C67.1, C69.1, C71.2, C72.2, Q4.S1, R55.1, R70.1, R72.2, U15.HSRN
- net VCC: now also C62.2, C67.1, C69.1, C71.2, C72.2, Q4.S1, R55.1, R70.1, R72.2, U15.HSRN
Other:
- note added: "IMU"
- note added: "Motor Controllers, Servo"
- note removed: "Motor Controllers"
- moved on the sheet: LED3, R23, R25
